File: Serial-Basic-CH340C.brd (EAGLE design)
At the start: 21.6 x 16.5 mm, 43 parts, among them U1 AP2112-3.3V, U5 CH340C

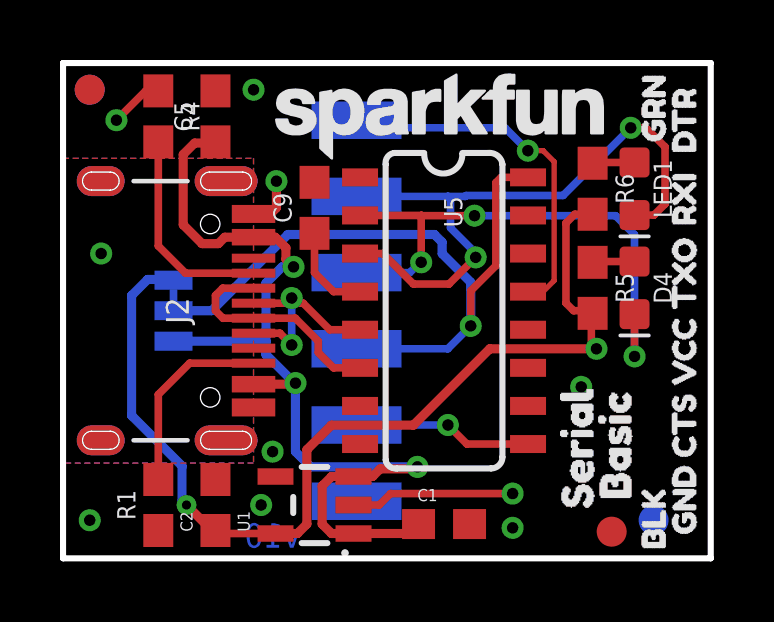
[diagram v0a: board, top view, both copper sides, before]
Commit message: Updating libraries, tidied up schematic, deleted unneccessary files, adding readme outline
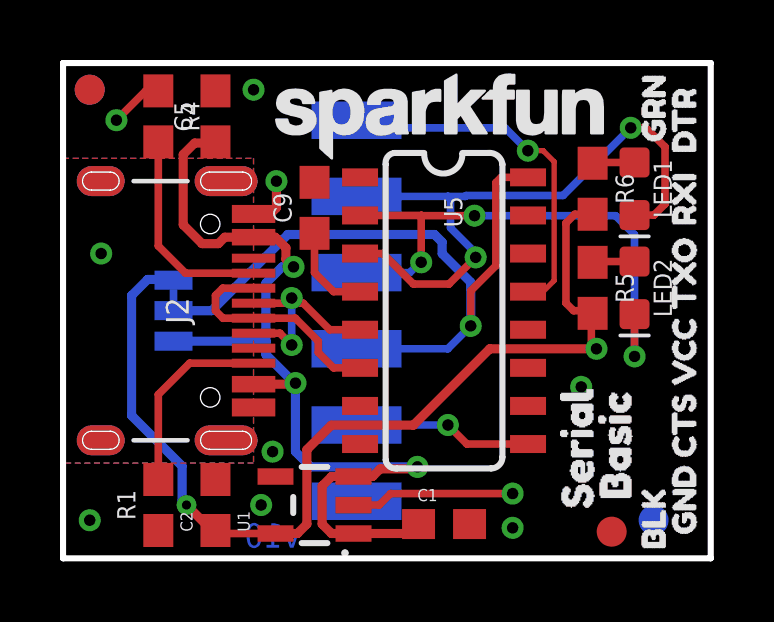
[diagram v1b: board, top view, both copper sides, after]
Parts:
- J2: device USB-C:USB-C-16P -> SparkFun-Connectors:USB-C-16P
- U1: value AP2112-3.3V -> 3.3V; device SparkFun-PowerIC:SOT23-5 -> SparkFun-IC-Power:SOT23-5
- renumbered D4 to LED2
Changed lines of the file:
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@@
 <drawing>
 <settings>
-<setting alwaysvectorfont="yes"/>
+<setting alwaysvectorfont="no"/>
 <setting keepoldvectorfont="yes"/>
 <setting verticaltext="up"/>
@@
 <layers>
 <layer number="1" name="Top" color="4" fill="1" visible="yes" active="yes"/>
-<layer number="16" name="Bottom" color="1" fill="1" visible="yes" active="yes"/>
-<layer number="17" name="Pads" color="2" fill="1" visible="yes" active="yes"/>
+<layer number="16" name="Bottom" color="31" fill="1" visible="yes" active="yes"/>
+<layer number="17" name="Pads" color="30" fill="1" visible="yes" active="yes"/>
 <layer number="18" name="Vias" color="2" fill="1" visible="yes" active="yes"/>
 <layer number="19" name="Unrouted" color="6" fill="1" visible="yes" active="yes"/>
-<layer number="20" name="Dimension" color="24" fill="1" visible="yes" active="yes"/>
+<layer number="20" name="Dimension" color="15" fill="1" visible="yes" active="yes"/>
 <layer number="21" name="tPlace" color="16" fill="1" visible="yes" active="yes"/>
 <layer number="22" name="bPlace" color="14" fill="1" visible="yes" active="yes"/>
@@
 <layer number="47" name="Measures" color="7" fill="1" visible="no" active="yes"/>
 <layer number="48" name="Document" color="7" fill="1" visible="no" active="yes"/>
-<layer number="49" name="Reference" color="7" fill="1" visible="no" active="yes"/>
+<layer number="49" name="Reference" color="13" fill="1" visible="yes" active="yes"/>
 <layer number="50" name="dxf" color="7" fill="1" visible="no" active="yes"/>
 <layer number="51" name="tDocu" color="6" fill="1" visible="yes" active="yes"/>
@@
 <layer number="115" name="ReferenceISLANDS" color="7" fill="1" visible="no" active="no"/>
 <layer number="116" name="Patch_BOT" color="9" fill="4" visible="no" active="no"/>
+<layer number="117" name="PM_Ref" color="26" fill="1" visible="yes" active="yes"/>
 <layer number="118" name="Rect_Pads" color="7" fill="1" visible="no" active="no"/>
+<layer number="119" name="PF_Ref" color="31" fill="1" visible="yes" active="yes"/>
+<layer number="120" name="WFL_Ref" color="25" fill="1" visible="yes" active="yes"/>
 <layer number="121" name="_tsilk" color="7" fill="1" visible="no" active="no"/>
 <layer number="122" name="_bsilk" color="7" fill="1" visible="no" active="no"/>
@@
 </element>
 <element name="LOGO1" library="SparkFun-Aesthetics" package="OSHW-LOGO-S" value="OSHW-LOGOS" x="3.302" y="14.605" smashed="yes" rot="MR0"/>
-<element name="U1" library="SparkFun-PowerIC" package="SOT23-5" value="AP2112-3.3V" x="8.382" y="1.778" smashed="yes" rot="R90">
+<element name="U1" library="SparkFun-IC-Power" package="SOT23-5" value="3.3V" x="8.382" y="1.778" smashed="yes" rot="R90">
 <attribute name="NAME" x="6.223" y="0.889" size="0.4064" layer="25" rot="R90"/>
 <attribute name="PROD_ID" value="VREG-12457" x="8.382" y="1.778" size="1.778" layer="27" font="vector" ratio="15" rot="R90" display="off"/>
+<attribute name="VALUE" value="3.3V" x="8.382" y="1.778" size="1.778" layer="27" rot="R90" display="off"/>
 <attribute name="VALUE" x="8.5725" y="0.8255" size="0.4064" layer="27" rot="R90"/>
 </element>
@@
 <attribute name="VALUE" x="5.842" y="14.732" size="0.6096" layer="27" font="vector" ratio="20" rot="R90" align="top-center"/>
 </element>
-<element name="D4" library="SparkFun-LED" package="LED-0603" value="Yellow" x="19.05" y="9.017" smashed="yes" rot="R270">
+<element name="LED2" library="SparkFun-LED" package="LED-0603" value="Yellow" x="19.05" y="9.017" smashed="yes" rot="R270">
 <attribute name="NAME" x="19.685" y="9.017" size="0.6096" layer="25" font="vector" ratio="20" rot="R270" align="bottom-center"/>
 <attribute name="PROD_ID" value="DIO-09003" x="3.81" y="31.877" size="1.778" layer="27" font="vector" ratio="15" rot="R270" display="off"/>
@@
 <element name="U$5" library="buzzard_labels (5)" package="TXO0" value="" x="20.701" y="7.62" smashed="yes" rot="R90"/>
 <element name="U$6" library="buzzard_labels (5)" package="VCC2" value="" x="20.701" y="4.953" smashed="yes" rot="R90"/>
-<element name="J2" library="USB-C" package="USB-C-16P" value="" x="6.35" y="8.255" smashed="yes" rot="R270">
+<element name="J2" library="SparkFun-Connectors" package="USB-C-16P" value="" x="6.35" y="8.255" smashed="yes" rot="R270">
 <attribute name="NAME" x="3.81" y="8.255" size="0.762" layer="25" rot="R270" align="center"/>
+<attribute name="PROD_ID" value="CONN-14122" x="6.35" y="8.255" size="1.778" layer="27" rot="R270" display="off"/>
 <attribute name="VALUE" x="2.54" y="8.255" size="0.762" layer="27" rot="R270" align="center"/>
 </element>
@@
 </signal>
 <signal name="N$11">
-<contactref element="D4" pad="A"/>
+<contactref element="LED2" pad="A"/>
 <contactref element="R5" pad="1"/>
 <wire x1="19.05" y1="9.894" x2="17.68" y2="9.894" width="0.254" layer="1"/>
@@
 <signal name="TXO">
 <contactref element="J1" pad="4"/>
-<contactref element="D4" pad="C"/>
+<contactref element="LED2" pad="C"/>
 <contactref element="U5" pad="2"/>
 <via x="13.716" y="11.4221" extent="1-16" drill="0.381"/>
